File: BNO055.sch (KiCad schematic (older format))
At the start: 6 parts, among them U2 BNO055, Y1 32.768kHz

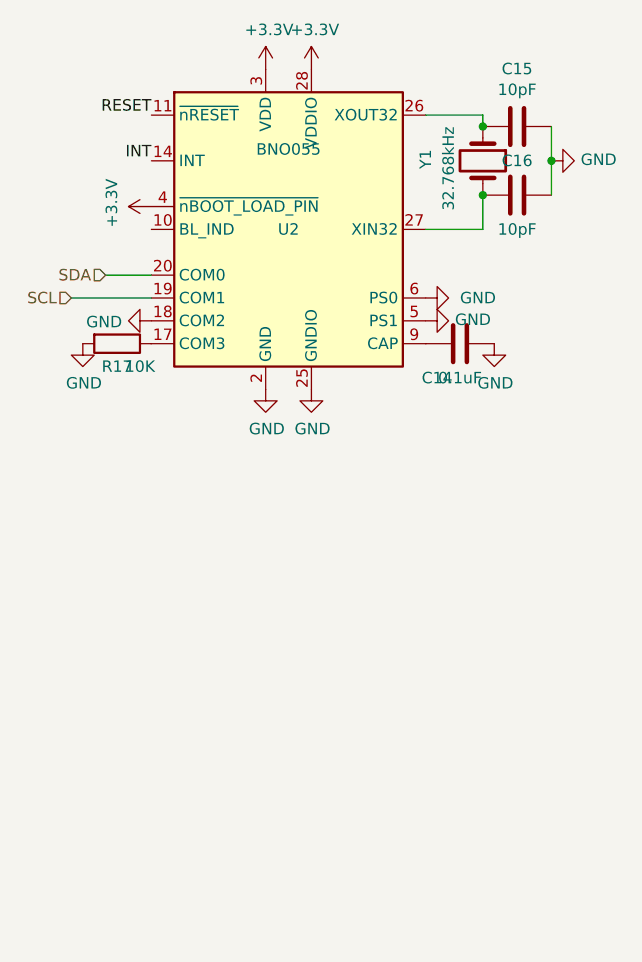
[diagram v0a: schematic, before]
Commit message: added cm4
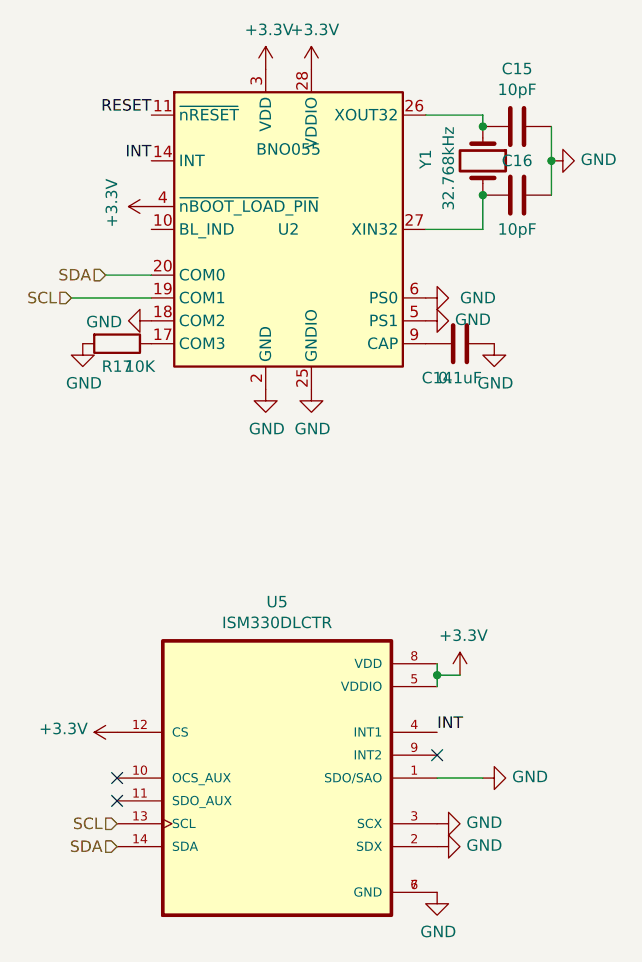
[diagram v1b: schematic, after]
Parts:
- added U5: ISM330DLCTR, ISM330DLCTR:PQFN50P250X300X86-14N, symbol ISM330DLCTR:ISM330DLCTR
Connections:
- net +3V3: now also U5.12 (CS), U5.5 (VDDIO), U5.8 (VDD)
- net GND: now also U5.1 (SDO/SAO), U5.2 (SDX), U5.3 (SCX), U5.6 (GND), U5.7 (GND)
- net INT: now also U5.4 (INT1)
- net SCL: now also U5.13 (SCL)
- net SDA: now also U5.14 (SDA)
- no-connect marks 0 -> 3
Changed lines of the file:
@@
 Text HLabel 4400 3850 0    50   Input ~ 0
 SCL
+$Comp
+L ISM330DLCTR:ISM330DLCTR U5
+U 1 1 60DA4B59
+P 5300 5950
+F 0 "U5" H 5300 6720 50  0000 C CNN
+F 1 "ISM330DLCTR" H 5300 6629 50  0000 C CNN
+F 2 "ISM330DLCTR:PQFN50P250X300X86-14N" H 5300 5950 50  0001 L BNN
+F 3 "" H 5300 5950 50  0001 L BNN
+F 4 "IPC-7351B" H 5300 5950 50  0001 L BNN "STANDARD"
+F 5 "2" H 5300 5950 50  0001 L BNN "PARTREV"
+F 6 "STMicroelectronics" H 5300 5950 50  0001 L BNN "MANUFACTURER"
+	1    5300 5950
+	1    0    0    -1
+$EndComp
+Wire Wire Line
+	6000 5450 6000 5500
+Wire Wire Line
+	6000 5500 6100 5500
+Connection ~ 6000 5500
+Wire Wire Line
+	6000 5500 6000 5550
+$Comp
+L power:+3.3V #PWR0225
+U 1 1 60DA76CA
+P 6100 5500
+F 0 "#PWR0225" H 6100 5350 50  0001 C CNN
+F 1 "+3.3V" H 6115 5673 50  0000 C CNN
+F 2 "" H 6100 5500 50  0001 C CNN
+F 3 "" H 6100 5500 50  0001 C CNN
+	1    6100 5500
+	1    0    0    -1
+$EndComp
+Text HLabel 4600 6250 0    50   Input ~ 0
+SDA
+Text HLabel 4600 6150 0    50   Input ~ 0
+SCL
+NoConn ~ 4600 6050
+NoConn ~ 4600 5950
+NoConn ~ 6000 5850
+$Comp
+L power:GND #PWR0226
+U 1 1 60DAA531
+P 6000 6450
+F 0 "#PWR0226" H 6000 6200 50  0001 C CNN
+F 1 "GND" H 6005 6277 50  0000 C CNN
+F 2 "" H 6000 6450 50  0001 C CNN
+F 3 "" H 6000 6450 50  0001 C CNN
+	1    6000 6450
+	1    0    0    -1
+$EndComp
+Text Label 6000 5750 0    50   ~ 0
+INT
+Wire Wire Line
+	6000 5950 6200 5950
+$Comp
+L power:GND #PWR0227
+U 1 1 60DACA73
+P 6200 5950
+F 0 "#PWR0227" H 6200 5700 50  0001 C CNN
+F 1 "GND" V 6205 5822 50  0000 R CNN
+F 2 "" H 6200 5950 50  0001 C CNN
+F 3 "" H 6200 5950 50  0001 C CNN
+	1    6200 5950
+	0    -1   -1   0
+$EndComp
+$Comp
+L power:GND #PWR0228
+U 1 1 60DAD5CC
+P 6000 6150
+F 0 "#PWR0228" H 6000 5900 50  0001 C CNN
+F 1 "GND" V 6005 6022 50  0000 R CNN
+F 2 "" H 6000 6150 50  0001 C CNN
+F 3 "" H 6000 6150 50  0001 C CNN
+	1    6000 6150
+	0    -1   -1   0
+$EndComp
+$Comp
+L power:GND #PWR0229
+U 1 1 60DAD8C3
+P 6000 6250
+F 0 "#PWR0229" H 6000 6000 50  0001 C CNN
+F 1 "GND" V 6005 6122 50  0000 R CNN
+F 2 "" H 6000 6250 50  0001 C CNN
+F 3 "" H 6000 6250 50  0001 C CNN
+	1    6000 6250
+	0    -1   -1   0
+$EndComp
+$Comp
+L power:+3.3V #PWR0230
+U 1 1 60DAE1F7
+P 4600 5750
+F 0 "#PWR0230" H 4600 5600 50  0001 C CNN
+F 1 "+3.3V" V 4615 5878 50  0000 L CNN
+F 2 "" H 4600 5750 50  0001 C CNN
+F 3 "" H 4600 5750 50  0001 C CNN
+	1    4600 5750
+	0    -1   -1   0
+$EndComp
 $EndSCHEMATC
